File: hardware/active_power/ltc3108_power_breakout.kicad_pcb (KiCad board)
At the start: 2 copper layers, 77 x 57 mm, 13 parts, among them J1 TEG, J2 External_LPR6235_752SML, J3 OUT_3V3_LAB, J4 EXTERNAL_VSTORE_SUPERCAP_6V3, J5 PGOOD_MONITOR, U1 LTC3108EGN

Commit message: hardware: route vendor-reference LTC3108 C1/C2 pump paths on active PCB prototype candidate
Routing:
- net PMIC_C1: track 0.00 -> 43.0 mm
- net PMIC_C2: track 0.00 -> 25.3 mm
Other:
- board text added: "LTC3108 LAB POWER / PARTIAL ROUTE REV A0"
- board text removed: "LTC3108 LAB POWER / UNROUTED REV A0"
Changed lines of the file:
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@@
 (pad "2" thru_hole circle (at 0 2.54) (size 1.65 1.65) (drill 0.9) (layers "*.Cu" "*.Mask") (net 1 "GND"))
 )
+(segment (start 59.1 17) (end 66 17) (width 0.2) (layer "F.Cu") (net 8))
+(segment (start 66 17) (end 66 35.6825) (width 0.2) (layer "F.Cu") (net 8))
+(segment (start 66 35.6825) (end 48.6 35.6825) (width 0.2) (layer "F.Cu") (net 8))
+(segment (start 59.1 24) (end 61 24) (width 0.2) (layer "F.Cu") (net 9))
+(segment (start 61 24) (end 61 35.0475) (width 0.2) (layer "F.Cu") (net 9))
+(segment (start 61 35.0475) (end 48.6 35.0475) (width 0.2) (layer "F.Cu") (net 9))
 (gr_line (start 10 10) (end 87 10) (stroke (width 0.05) (type default)) (layer "Edge.Cuts"))
 (gr_line (start 87 10) (end 87 67) (stroke (width 0.05) (type default)) (layer "Edge.Cuts"))
@@
 (gr_line (start 10 67) (end 10 10) (stroke (width 0.05) (type default)) (layer "Edge.Cuts"))
 (gr_text "MOJEATEREGO (C) 2026 A. MIKULSKI" (at 48 58) (layer "B.SilkS") (effects (font (size 0.85 0.85) (thickness 0.13)) (justify mirror)))
-(gr_text "LTC3108 LAB POWER / UNROUTED REV A0" (at 46 63) (layer "F.SilkS") (effects (font (size 1 1) (thickness 0.15))))
+(gr_text "LTC3108 LAB POWER / PARTIAL ROUTE REV A0" (at 46 63) (layer "F.SilkS") (effects (font (size 1 1) (thickness 0.15))))
 )

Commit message: hardware: route existing LTC3108 reference TEG input, regulated output, VSTORE and ground connectors
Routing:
- net GND: track 0.00 -> 93.1 mm
- net TEG_P: track 0.00 -> 45.0 mm
- net VOUT: track 0.00 -> 25.0 mm
- net VSTORE: track 0.00 -> 14.0 mm
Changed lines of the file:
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@@
 (segment (start 61 24) (end 61 35.0475) (width 0.2) (layer "F.Cu") (net 9))
 (segment (start 61 35.0475) (end 48.6 35.0475) (width 0.2) (layer "F.Cu") (net 9))
+(segment (start 15 21) (end 25 21) (width 0.35) (layer "F.Cu") (net 11))
+(segment (start 15 23.54) (end 25 23.54) (width 0.35) (layer "F.Cu") (net 1))
+(segment (start 15 42) (end 27 42) (width 0.35) (layer "B.Cu") (net 11))
+(segment (start 27 42) (end 27 21) (width 0.35) (layer "B.Cu") (net 11))
+(segment (start 27 21) (end 25 21) (width 0.35) (layer "B.Cu") (net 11))
+(segment (start 15 49.62) (end 13 49.62) (width 0.35) (layer "B.Cu") (net 1))
+(segment (start 13 49.62) (end 13 23.54) (width 0.35) (layer "B.Cu") (net 1))
+(segment (start 13 23.54) (end 25 23.54) (width 0.35) (layer "B.Cu") (net 1))
+(segment (start 79 21) (end 72 21) (width 0.35) (layer "F.Cu") (net 4))
+(segment (start 72 21) (end 72 35) (width 0.35) (layer "F.Cu") (net 4))
+(segment (start 72 35) (end 68 35) (width 0.35) (layer "F.Cu") (net 4))
+(segment (start 79 42) (end 74 42) (width 0.35) (layer "F.Cu") (net 3))
+(segment (start 74 42) (end 74 45) (width 0.35) (layer "F.Cu") (net 3))
+(segment (start 74 45) (end 68 45) (width 0.35) (layer "F.Cu") (net 3))
+(segment (start 68 37.54) (end 64 37.54) (width 0.3) (layer "B.Cu") (net 1))
+(segment (start 64 37.54) (end 64 47.54) (width 0.3) (layer "B.Cu") (net 1))
+(segment (start 64 47.54) (end 68 47.54) (width 0.3) (layer "B.Cu") (net 1))
+(segment (start 79 23.54) (end 76 23.54) (width 0.3) (layer "B.Cu") (net 1))
+(segment (start 76 23.54) (end 76 37.54) (width 0.3) (layer "B.Cu") (net 1))
+(segment (start 76 37.54) (end 68 37.54) (width 0.3) (layer "B.Cu") (net 1))
 (gr_line (start 10 10) (end 87 10) (stroke (width 0.05) (type default)) (layer "Edge.Cuts"))
 (gr_line (start 87 10) (end 87 67) (stroke (width 0.05) (type default)) (layer "Edge.Cuts"))

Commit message: hardware: route manufacturer-reference transformer secondary to both LTC3108 charge pump capacitor inputs
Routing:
- net SEC_HI: track 0.00 -> 81.7 mm, vias 0 -> 2
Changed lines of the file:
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@@
 (segment (start 76 23.54) (end 76 37.54) (width 0.3) (layer "B.Cu") (net 1))
 (segment (start 76 37.54) (end 68 37.54) (width 0.3) (layer "B.Cu") (net 1))
+(segment (start 56.9 17) (end 55 17) (width 0.2) (layer "F.Cu") (net 12))
+(segment (start 56.9 24) (end 55 24) (width 0.2) (layer "F.Cu") (net 12))
+(segment (start 55 17) (end 55 24) (width 0.3) (layer "B.Cu") (net 12))
+(segment (start 55 24) (end 55 51) (width 0.3) (layer "B.Cu") (net 12))
+(segment (start 55 51) (end 20 51) (width 0.3) (layer "B.Cu") (net 12))
+(segment (start 20 51) (end 20 47.08) (width 0.3) (layer "B.Cu") (net 12))
+(segment (start 20 47.08) (end 15 47.08) (width 0.3) (layer "B.Cu") (net 12))
+(via (at 55 17) (size 0.8) (drill 0.4) (layers "F.Cu" "B.Cu") (net 12))
+(via (at 55 24) (size 0.8) (drill 0.4) (layers "F.Cu" "B.Cu") (net 12))
 (gr_line (start 10 10) (end 87 10) (stroke (width 0.05) (type default)) (layer "Edge.Cuts"))
 (gr_line (start 87 10) (end 87 67) (stroke (width 0.05) (type default)) (layer "Edge.Cuts"))

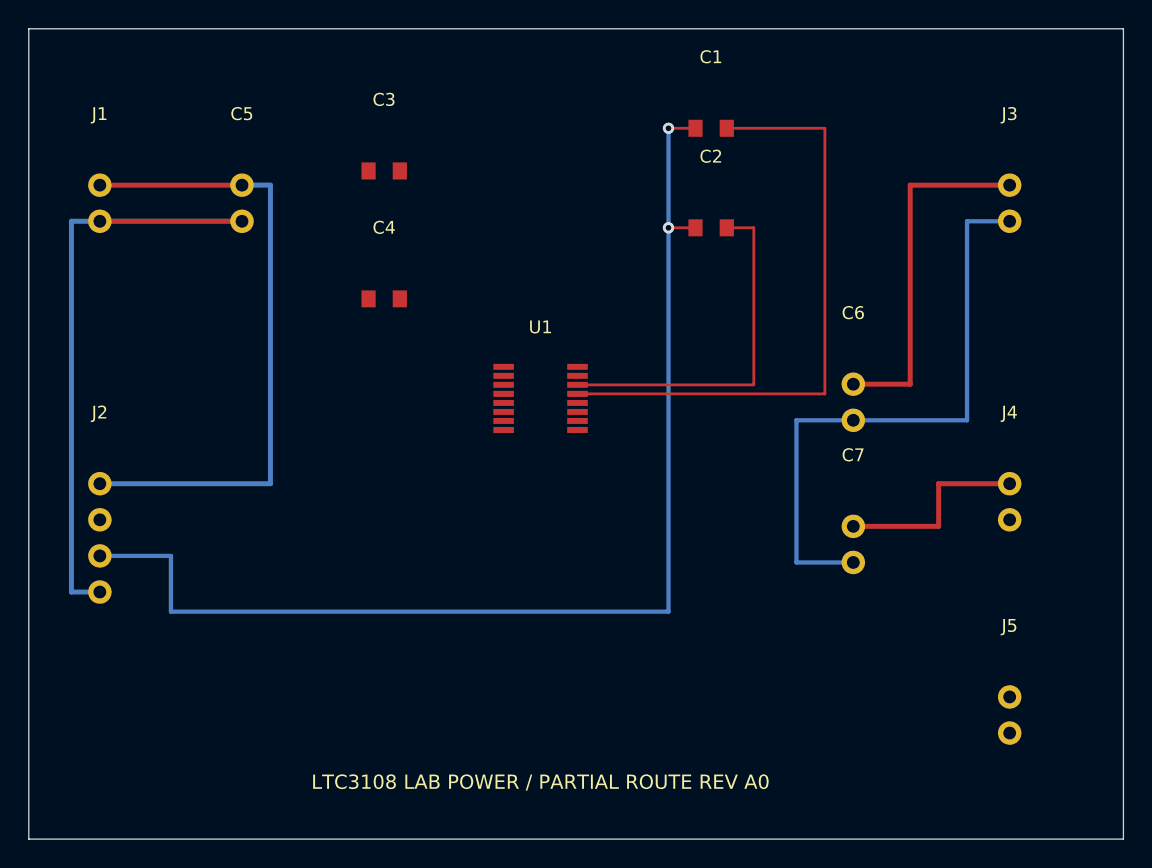
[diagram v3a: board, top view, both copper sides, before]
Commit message: fix(cad): remove duplicate parallel transformer secondary route; retain tested two-via reference network
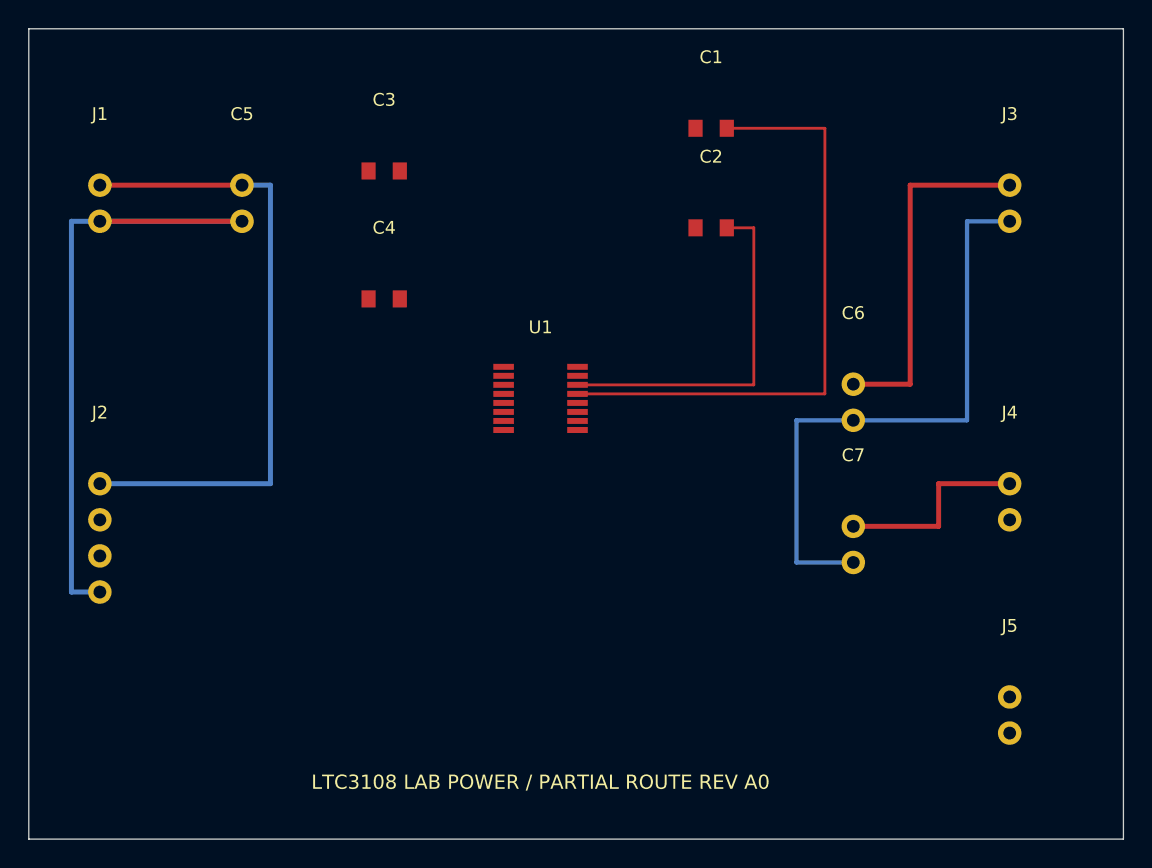
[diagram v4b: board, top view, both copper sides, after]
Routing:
- net SEC_HI: track 81.7 -> 0.00 mm, vias 2 -> 0
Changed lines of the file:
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@@
 (segment (start 76 23.54) (end 76 37.54) (width 0.3) (layer "B.Cu") (net 1))
 (segment (start 76 37.54) (end 68 37.54) (width 0.3) (layer "B.Cu") (net 1))
-(segment (start 56.9 17) (end 55 17) (width 0.2) (layer "F.Cu") (net 12))
-(segment (start 56.9 24) (end 55 24) (width 0.2) (layer "F.Cu") (net 12))
-(segment (start 55 17) (end 55 24) (width 0.3) (layer "B.Cu") (net 12))
-(segment (start 55 24) (end 55 51) (width 0.3) (layer "B.Cu") (net 12))
-(segment (start 55 51) (end 20 51) (width 0.3) (layer "B.Cu") (net 12))
-(segment (start 20 51) (end 20 47.08) (width 0.3) (layer "B.Cu") (net 12))
-(segment (start 20 47.08) (end 15 47.08) (width 0.3) (layer "B.Cu") (net 12))
-(via (at 55 17) (size 0.8) (drill 0.4) (layers "F.Cu" "B.Cu") (net 12))
-(via (at 55 24) (size 0.8) (drill 0.4) (layers "F.Cu" "B.Cu") (net 12))
 (gr_line (start 10 10) (end 87 10) (stroke (width 0.05) (type default)) (layer "Edge.Cuts"))
 (gr_line (start 87 10) (end 87 67) (stroke (width 0.05) (type default)) (layer "Edge.Cuts"))

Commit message: fix(cad): restore exactly one two-via LTC3108 transformer secondary route after simultaneous edits
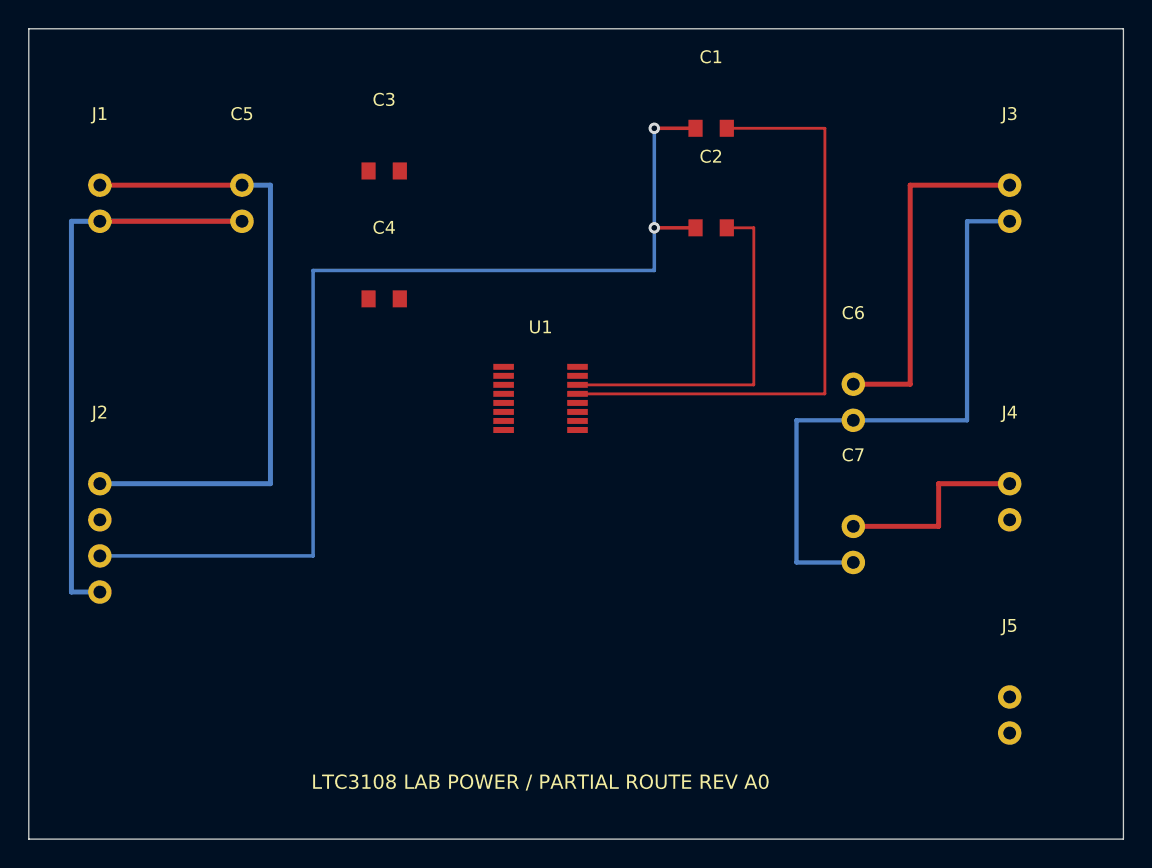
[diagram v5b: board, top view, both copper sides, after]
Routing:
- net SEC_HI: track 0.00 -> 74.9 mm, vias 0 -> 2
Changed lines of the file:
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@@
 (segment (start 76 23.54) (end 76 37.54) (width 0.3) (layer "B.Cu") (net 1))
 (segment (start 76 37.54) (end 68 37.54) (width 0.3) (layer "B.Cu") (net 1))
+(segment (start 56.9 17) (end 54 17) (width 0.25) (layer "F.Cu") (net 12))
+(segment (start 56.9 24) (end 54 24) (width 0.25) (layer "F.Cu") (net 12))
+(segment (start 54 17) (end 54 24) (width 0.25) (layer "B.Cu") (net 12))
+(segment (start 15 47.08) (end 30 47.08) (width 0.25) (layer "B.Cu") (net 12))
+(segment (start 30 47.08) (end 30 27) (width 0.25) (layer "B.Cu") (net 12))
+(segment (start 30 27) (end 54 27) (width 0.25) (layer "B.Cu") (net 12))
+(segment (start 54 27) (end 54 24) (width 0.25) (layer "B.Cu") (net 12))
+(via (at 54 17) (size 0.8) (drill 0.4) (layers "F.Cu" "B.Cu") (net 12))
+(via (at 54 24) (size 0.8) (drill 0.4) (layers "F.Cu" "B.Cu") (net 12))
 (gr_line (start 10 10) (end 87 10) (stroke (width 0.05) (type default)) (layer "Edge.Cuts"))
 (gr_line (start 87 10) (end 87 67) (stroke (width 0.05) (type default)) (layer "Edge.Cuts"))
